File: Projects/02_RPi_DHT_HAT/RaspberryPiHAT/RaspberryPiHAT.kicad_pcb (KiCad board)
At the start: 2 copper layers, 9 parts, among them J1 Raspberry_Pi_2_3, SW1 SW_DPST, U1 DHT22

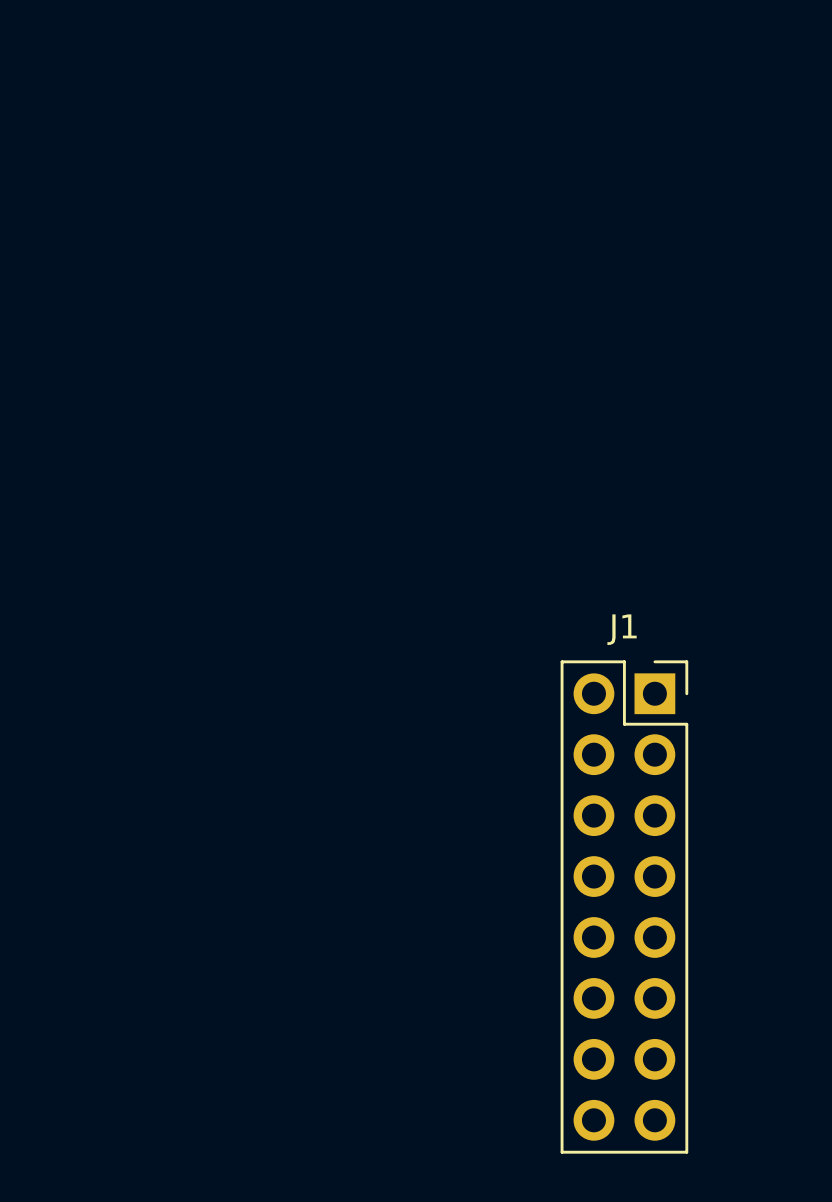
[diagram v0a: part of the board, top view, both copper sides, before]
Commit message: Project 2: Create PCB outline and mounting hole
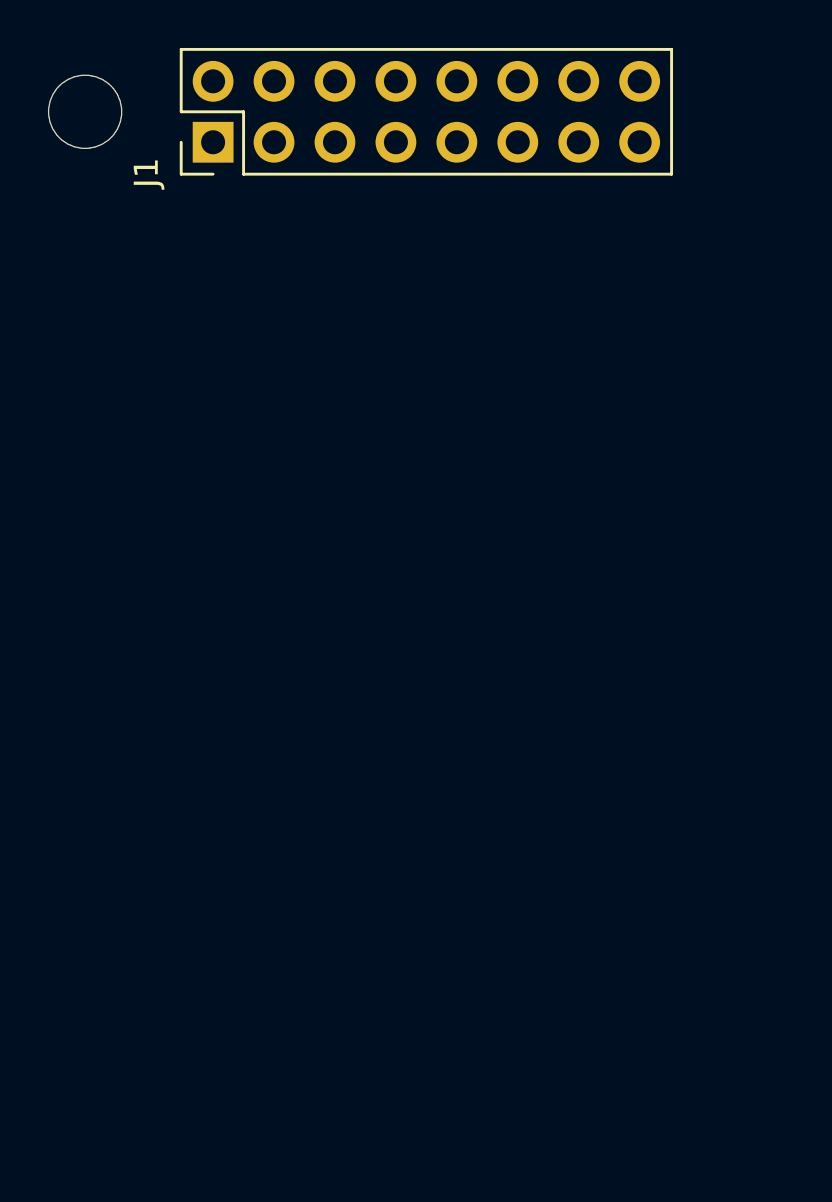
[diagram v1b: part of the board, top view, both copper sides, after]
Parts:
- J1: footprint Connector_PinSocket_2.54mm:PinSocket_2x08_P2.54mm_Vertical -> Connector_PinHeader_2.54mm:PinHeader_2x08_P2.54mm_Vertical
- moved J1 29.5 mm to (205.1, 63.1), turned to 90 degrees
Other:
- board outline added: 3 x 3 mm
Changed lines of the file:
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@@
   (general
     (thickness 1.6)
-    (drawings 0)
+    (drawings 1)
     (tracks 0)
     (zones 0)
@@
     (add_net GND)
   )
+  (module Connector_PinHeader_2.54mm:PinHeader_2x08_P2.54mm_Vertical (layer F.Cu)
+    (at 205.105 63.119 90)
+    (descr "Through hole straight pin header, 2x08, 2.54mm pitch, double rows")
+    (tags "Through hole pin header THT 2x08 2.54mm double row")
+    (fp_text reference J1 (at -1.27 -2.77 90) (layer F.SilkS)
+      (effects (font (size 1 1) (thickness 0.15)))
+    )
+    (fp_text value Raspberry_Pi_2_3 (at -1.27 20.55 90) (layer F.Fab)
+      (effects (font (size 1 1) (thickness 0.15)))
+    )
+    (fp_text user %R (at -1.27 8.89) (layer F.Fab)
+      (effects (font (size 1 1) (thickness 0.15)))
+    )
+    (fp_line (start 0 -1.27) (end 3.81 -1.27) (layer F.Fab) (width 0.1))
+    (fp_line (start 3.81 -1.27) (end 3.81 19.05) (layer F.Fab) (width 0.1))
+    (fp_line (start 3.81 19.05) (end -1.27 19.05) (layer F.Fab) (width 0.1))
+    (fp_line (start -1.27 19.05) (end -1.27 0) (layer F.Fab) (width 0.1))
+    (fp_line (start -1.27 0) (end 0 -1.27) (layer F.Fab) (width 0.1))
+    (fp_line (start -1.33 19.11) (end 3.87 19.11) (layer F.SilkS) (width 0.12))
+    (fp_line (start -1.33 1.27) (end -1.33 19.11) (layer F.SilkS) (width 0.12))
+    (fp_line (start 3.87 -1.33) (end 3.87 19.11) (layer F.SilkS) (width 0.12))
+    (fp_line (start -1.33 1.27) (end 1.27 1.27) (layer F.SilkS) (width 0.12))
+    (fp_line (start 1.27 1.27) (end 1.27 -1.33) (layer F.SilkS) (width 0.12))
+    (fp_line (start 1.27 -1.33) (end 3.87 -1.33) (layer F.SilkS) (width 0.12))
+    (fp_line (start -1.33 0) (end -1.33 -1.33) (layer F.SilkS) (width 0.12))
+    (fp_line (start -1.33 -1.33) (end 0 -1.33) (layer F.SilkS) (width 0.12))
+    (fp_line (start -1.8 -1.8) (end -1.8 19.55) (layer F.CrtYd) (width 0.05))
+    (fp_line (start -1.8 19.55) (end 4.35 19.55) (layer F.CrtYd) (width 0.05))
+    (fp_line (start 4.35 19.55) (end 4.35 -1.8) (layer F.CrtYd) (width 0.05))
+    (fp_line (start 4.35 -1.8) (end -1.8 -1.8) (layer F.CrtYd) (width 0.05))
+    (pad 16 thru_hole oval (at 2.54 17.78 90) (size 1.7 1.7) (drill 1) (layers *.Cu *.Mask)
+      (net 17 "Net-(J1-Pad16)"))
+    (pad 15 thru_hole oval (at 0 17.78 90) (size 1.7 1.7) (drill 1) (layers *.Cu *.Mask)
+      (net 16 "Net-(J1-Pad15)"))
+    (pad 14 thru_hole oval (at 2.54 15.24 90) (size 1.7 1.7) (drill 1) (layers *.Cu *.Mask)
+      (net 15 "Net-(J1-Pad14)"))
+    (pad 13 thru_hole oval (at 0 15.24 90) (size 1.7 1.7) (drill 1) (layers *.Cu *.Mask)
+      (net 14 "Net-(J1-Pad13)"))
+    (pad 12 thru_hole oval (at 2.54 12.7 90) (size 1.7 1.7) (drill 1) (layers *.Cu *.Mask)
+      (net 13 "Net-(J1-Pad12)"))
+    (pad 11 thru_hole oval (at 0 12.7 90) (size 1.7 1.7) (drill 1) (layers *.Cu *.Mask)
+      (net 12 "Net-(J1-Pad11)"))
+    (pad 10 thru_hole oval (at 2.54 10.16 90) (size 1.7 1.7) (drill 1) (layers *.Cu *.Mask)
+      (net 11 "Net-(J1-Pad10)"))
+    (pad 9 thru_hole oval (at 0 10.16 90) (size 1.7 1.7) (drill 1) (layers *.Cu *.Mask)
+      (net 1 GND))
+    (pad 8 thru_hole oval (at 2.54 7.62 90) (size 1.7 1.7) (drill 1) (layers *.Cu *.Mask)
+      (net 10 /button_input))
+    (pad 7 thru_hole oval (at 0 7.62 90) (size 1.7 1.7) (drill 1) (layers *.Cu *.Mask)
+      (net 9 "Net-(J1-Pad7)"))
+    (pad 6 thru_hole oval (at 2.54 5.08 90) (size 1.7 1.7) (drill 1) (layers *.Cu *.Mask)
+      (net 1 GND))
+    (pad 5 thru_hole oval (at 0 5.08 90) (size 1.7 1.7) (drill 1) (layers *.Cu *.Mask)
+      (net 8 "Net-(J1-Pad5)"))
+    (pad 4 thru_hole oval (at 2.54 2.54 90) (size 1.7 1.7) (drill 1) (layers *.Cu *.Mask)
+      (net 7 "Net-(J1-Pad4)"))
+    (pad 3 thru_hole oval (at 0 2.54 90) (size 1.7 1.7) (drill 1) (layers *.Cu *.Mask)
+      (net 6 "Net-(J1-Pad3)"))
+    (pad 2 thru_hole oval (at 2.54 0 90) (size 1.7 1.7) (drill 1) (layers *.Cu *.Mask)
+      (net 5 "Net-(J1-Pad2)"))
+    (pad 1 thru_hole rect (at 0 0 90) (size 1.7 1.7) (drill 1) (layers *.Cu *.Mask)
+      (net 4 /3V3))
+    (model ${KISYS3DMOD}/Connector_PinHeader_2.54mm.3dshapes/PinHeader_2x08_P2.54mm_Vertical.wrl
+      (at (xyz 0 0 0))
+      (scale (xyz 1 1 1))
+      (rotate (xyz 0 0 0))
+    )
+  )
   (module LED_SMD:LED_0805_2012Metric (layer F.Cu)
     (at 265.5085 69.215)
@@
       (net 1 GND))
     (model ${KISYS3DMOD}/LED_SMD.3dshapes/LED_0805_2012Metric.wrl
-      (at (xyz 0 0 0))
-      (scale (xyz 1 1 1))
-      (rotate (xyz 0 0 0))
-    )
-  )
-  (module Connector_PinSocket_2.54mm:PinSocket_2x08_P2.54mm_Vertical (layer F.Cu)
-    (at 223.52 86.106)
-    (descr "Through hole straight socket strip, 2x08, 2.54mm pitch, double cols (from Kicad 4.0.7), script generated")
-    (tags "Through hole socket strip THT 2x08 2.54mm double row")
-    (fp_text reference J1 (at -1.27 -2.77) (layer F.SilkS)
-      (effects (font (size 1 1) (thickness 0.15)))
-    )
-    (fp_text value Raspberry_Pi_2_3 (at -1.27 20.55) (layer F.Fab)
-      (effects (font (size 1 1) (thickness 0.15)))
-    )
-    (fp_line (start -4.34 19.55) (end -4.34 -1.8) (layer F.CrtYd) (width 0.05))
-    (fp_line (start 1.76 19.55) (end -4.34 19.55) (layer F.CrtYd) (width 0.05))
-    (fp_line (start 1.76 -1.8) (end 1.76 19.55) (layer F.CrtYd) (width 0.05))
-    (fp_line (start -4.34 -1.8) (end 1.76 -1.8) (layer F.CrtYd) (width 0.05))
-    (fp_line (start 0 -1.33) (end 1.33 -1.33) (layer F.SilkS) (width 0.12))
-    (fp_line (start 1.33 -1.33) (end 1.33 0) (layer F.SilkS) (width 0.12))
-    (fp_line (start -1.27 -1.33) (end -1.27 1.27) (layer F.SilkS) (width 0.12))
-    (fp_line (start -1.27 1.27) (end 1.33 1.27) (layer F.SilkS) (width 0.12))
-    (fp_line (start 1.33 1.27) (end 1.33 19.11) (layer F.SilkS) (width 0.12))
-    (fp_line (start -3.87 19.11) (end 1.33 19.11) (layer F.SilkS) (width 0.12))
-    (fp_line (start -3.87 -1.33) (end -3.87 19.11) (layer F.SilkS) (width 0.12))
-    (fp_line (start -3.87 -1.33) (end -1.27 -1.33) (layer F.SilkS) (width 0.12))
-    (fp_line (start -3.81 19.05) (end -3.81 -1.27) (layer F.Fab) (width 0.1))
-    (fp_line (start 1.27 19.05) (end -3.81 19.05) (layer F.Fab) (width 0.1))
-    (fp_line (start 1.27 -0.27) (end 1.27 19.05) (layer F.Fab) (width 0.1))
-    (fp_line (start 0.27 -1.27) (end 1.27 -0.27) (layer F.Fab) (width 0.1))
-    (fp_line (start -3.81 -1.27) (end 0.27 -1.27) (layer F.Fab) (width 0.1))
-    (fp_text user %R (at -1.27 8.89 90) (layer F.Fab)
-      (effects (font (size 1 1) (thickness 0.15)))
-    )
-    (pad 1 thru_hole rect (at 0 0) (size 1.7 1.7) (drill 1) (layers *.Cu *.Mask)
-      (net 4 /3V3))
-    (pad 2 thru_hole oval (at -2.54 0) (size 1.7 1.7) (drill 1) (layers *.Cu *.Mask)
-      (net 5 "Net-(J1-Pad2)"))
-    (pad 3 thru_hole oval (at 0 2.54) (size 1.7 1.7) (drill 1) (layers *.Cu *.Mask)
-      (net 6 "Net-(J1-Pad3)"))
-    (pad 4 thru_hole oval (at -2.54 2.54) (size 1.7 1.7) (drill 1) (layers *.Cu *.Mask)
-      (net 7 "Net-(J1-Pad4)"))
-    (pad 5 thru_hole oval (at 0 5.08) (size 1.7 1.7) (drill 1) (layers *.Cu *.Mask)
-      (net 8 "Net-(J1-Pad5)"))
-    (pad 6 thru_hole oval (at -2.54 5.08) (size 1.7 1.7) (drill 1) (layers *.Cu *.Mask)
-      (net 1 GND))
-    (pad 7 thru_hole oval (at 0 7.62) (size 1.7 1.7) (drill 1) (layers *.Cu *.Mask)
-      (net 9 "Net-(J1-Pad7)"))
-    (pad 8 thru_hole oval (at -2.54 7.62) (size 1.7 1.7) (drill 1) (layers *.Cu *.Mask)
-      (net 10 /button_input))
-    (pad 9 thru_hole oval (at 0 10.16) (size 1.7 1.7) (drill 1) (layers *.Cu *.Mask)
-      (net 1 GND))
-    (pad 10 thru_hole oval (at -2.54 10.16) (size 1.7 1.7) (drill 1) (layers *.Cu *.Mask)
-      (net 11 "Net-(J1-Pad10)"))
-    (pad 11 thru_hole oval (at 0 12.7) (size 1.7 1.7) (drill 1) (layers *.Cu *.Mask)
-      (net 12 "Net-(J1-Pad11)"))
-    (pad 12 thru_hole oval (at -2.54 12.7) (size 1.7 1.7) (drill 1) (layers *.Cu *.Mask)
-      (net 13 "Net-(J1-Pad12)"))
-    (pad 13 thru_hole oval (at 0 15.24) (size 1.7 1.7) (drill 1) (layers *.Cu *.Mask)
-      (net 14 "Net-(J1-Pad13)"))
-    (pad 14 thru_hole oval (at -2.54 15.24) (size 1.7 1.7) (drill 1) (layers *.Cu *.Mask)
-      (net 15 "Net-(J1-Pad14)"))
-    (pad 15 thru_hole oval (at 0 17.78) (size 1.7 1.7) (drill 1) (layers *.Cu *.Mask)
-      (net 16 "Net-(J1-Pad15)"))
-    (pad 16 thru_hole oval (at -2.54 17.78) (size 1.7 1.7) (drill 1) (layers *.Cu *.Mask)
-      (net 17 "Net-(J1-Pad16)"))
-    (model ${KISYS3DMOD}/Connector_PinSocket_2.54mm.3dshapes/PinSocket_2x08_P2.54mm_Vertical.wrl
       (at (xyz 0 0 0))
       (scale (xyz 1 1 1))
@@
     )
   )
+  (gr_circle (center 199.771 61.849) (end 198.247 61.849) (layer Edge.Cuts) (width 0.05))
 )

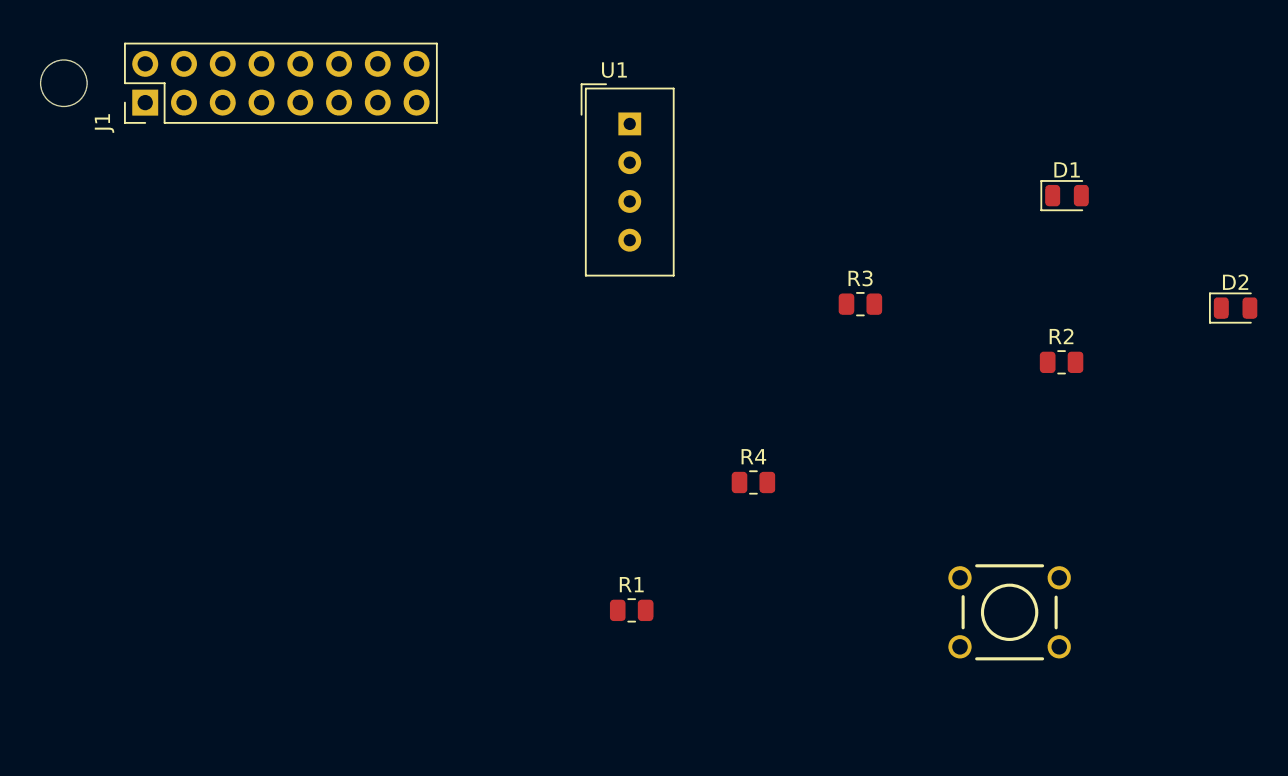
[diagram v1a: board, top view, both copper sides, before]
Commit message: Project 2: Place components on board and round PCB edges
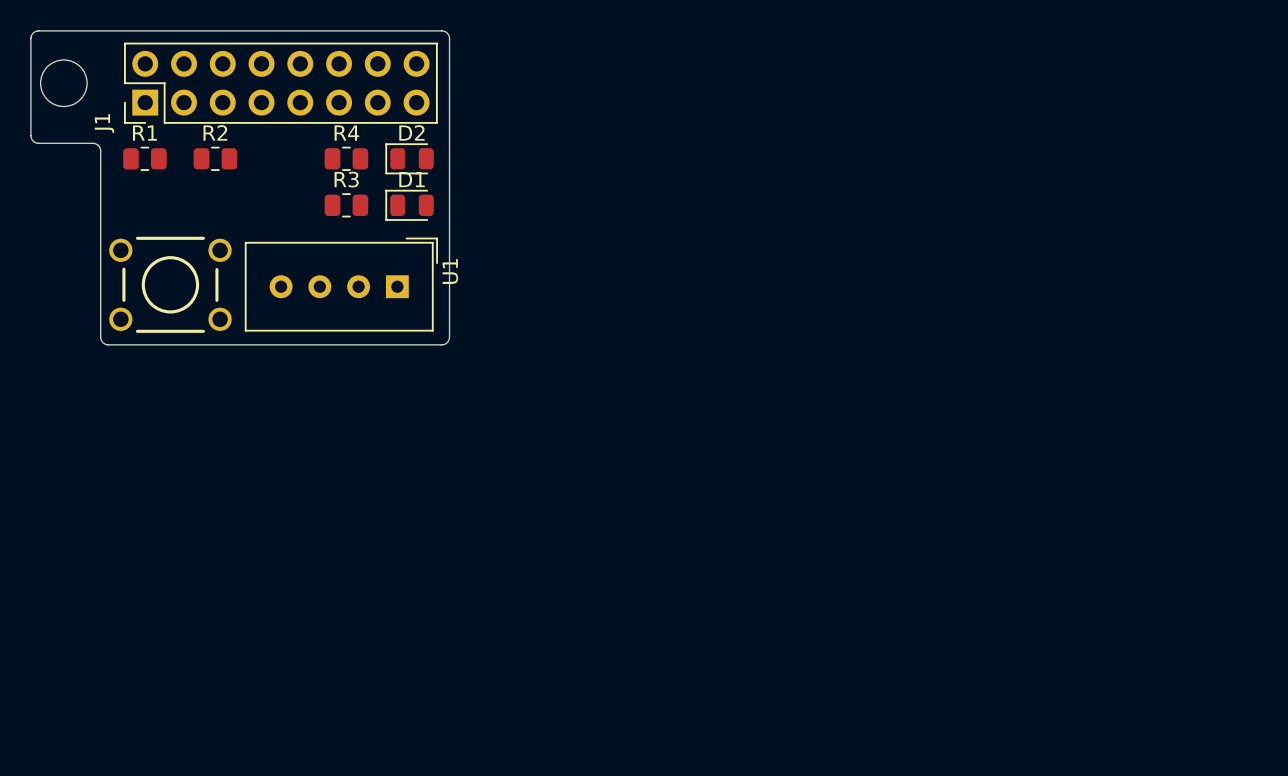
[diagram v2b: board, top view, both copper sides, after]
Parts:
- moved SW1 59.0 mm to (206.8, 75.1)
- moved R2 57.0 mm to (209.7, 66.8)
- moved D2 54.9 mm to (222.6, 66.8)
- moved R1 43.5 mm to (205.1, 66.8)
- moved D1 42.9 mm to (222.6, 69.8)
- moved R3 34.3 mm to (218.3, 69.8)
- moved R4 34.1 mm to (218.3, 66.8)
- moved U1 18.6 mm to (221.6, 75.2), turned to 270 degrees
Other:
- board size 3 x 3 mm -> 27.4 x 20.6 mm

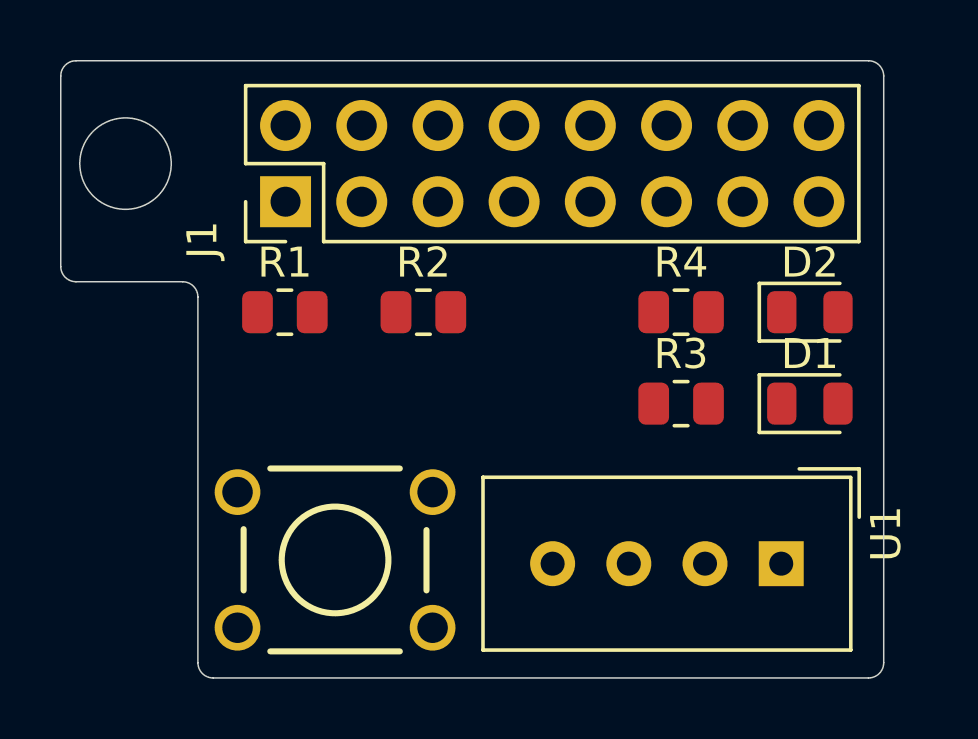
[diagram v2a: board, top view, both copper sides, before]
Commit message: Project 2: Route nets, critical traces, and power
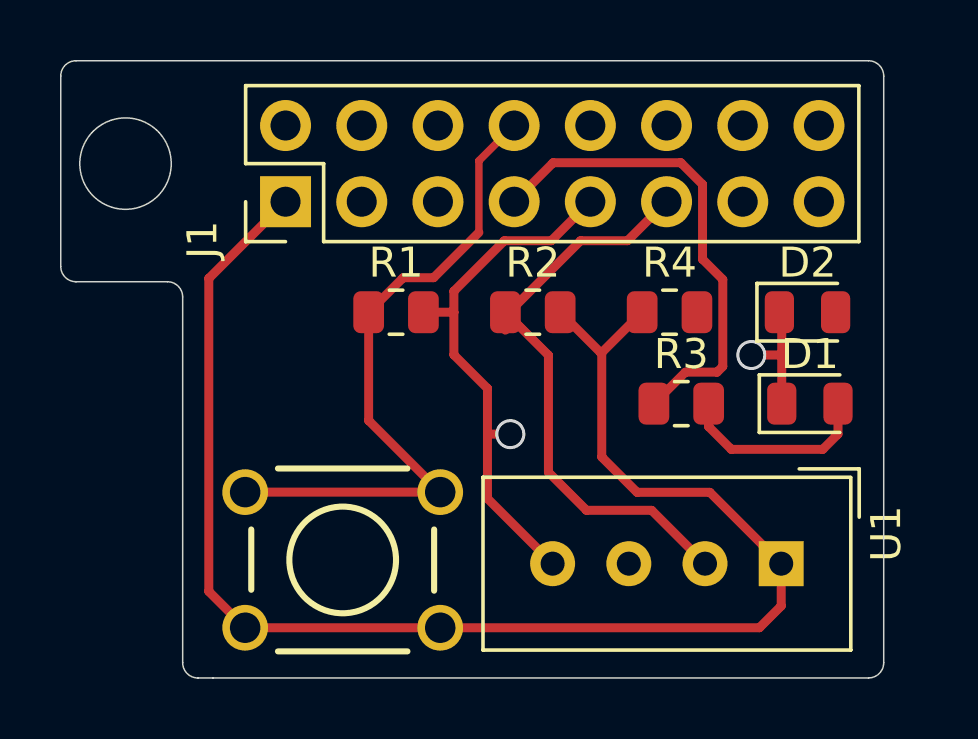
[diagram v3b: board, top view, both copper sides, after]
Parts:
- moved R1 3.71 mm to (208.8, 66.8)
- moved R2 3.65 mm to (213.3, 66.8)
- moved R4 0.38 mm to (217.9, 66.8)
- moved SW1 0.25 mm to (207.0, 75.1), turned to 180 degrees
- moved D2 0.08 mm to (222.5, 66.8)
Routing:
- net /3V3: track 0.00 -> 50.7 mm
- net /button_input: track 0.00 -> 22.3 mm
- net GND: track 0.00 -> 22.2 mm, vias 0 -> 2
- net Net-(J1-Pad11): track 0.00 -> 20.3 mm
- net Net-(J1-Pad7): track 0.00 -> 16.3 mm
- net Net-(D1-Pad2): track 0.00 -> 6.62 mm
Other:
- outline, holes or cut-outs redrawn

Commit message: Project 2: Reroute nets and add copper fill for GND plane
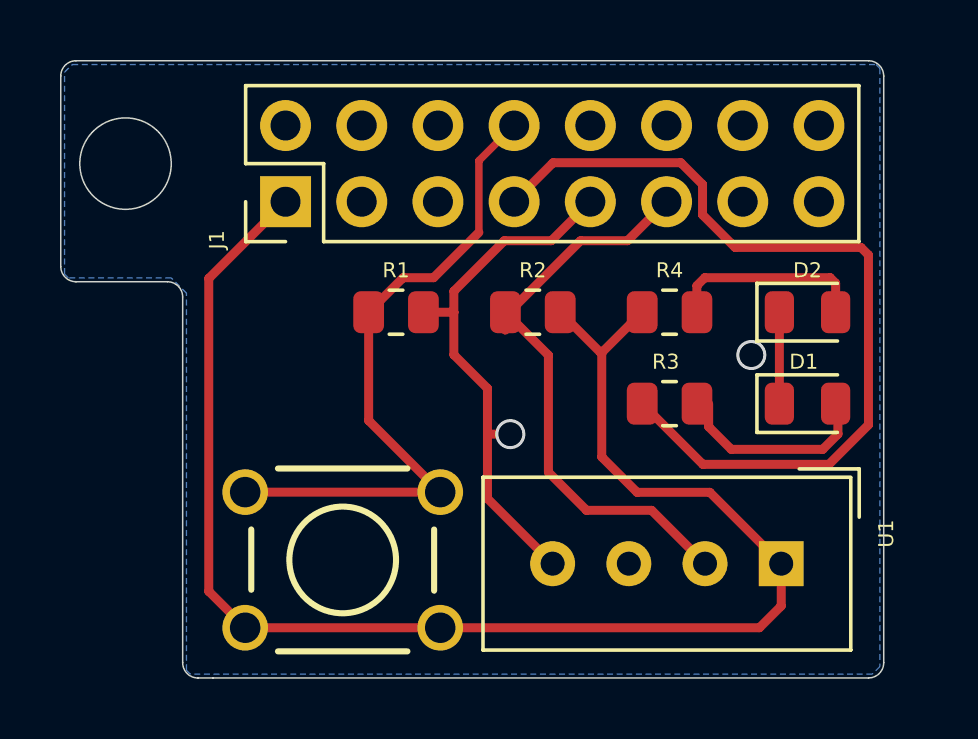
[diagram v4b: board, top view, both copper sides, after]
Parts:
- R1, R2: value R -> 10kΩ
- R3, R4: value R -> 330Ω
- moved R3 0.39 mm to (217.9, 69.8)
- moved D1 0.08 mm to (222.5, 69.8)
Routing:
- net Net-(J1-Pad7): track 16.3 -> 28.8 mm
- net Net-(D2-Pad2): track 0.00 -> 6.66 mm
- net GND: track 22.2 -> 21.1 mm
- added copper zone on B.Cu, net GND
